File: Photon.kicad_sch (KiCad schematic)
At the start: 55 parts, among them J1 USB_C_Receptacle_USB2.0_14P, Q1 IRLML6402, Q2 IRLML6402, SW1 TS-1088-AR02016, U1 ATtiny13A-S, U2 RT8059GJ5, U3 TP4056, U4 BCR421UW6-7, U5 DW01A, U6 FS8205A, U7 BCR421UW6-7

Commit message: Updated
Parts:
- C1, C2: value 4.7uF -> 10uF
- C7: value 0.1uF -> 100nF
- R18: value 10K -> 100K
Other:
- note added: "Voltage Regulator 3V3"
- note removed: "Voltage Regulator 3V6"
- moved on the sheet: BT1, C3, C6, C7, D1, D2, Q2, R10, R14, R17, R19, R7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

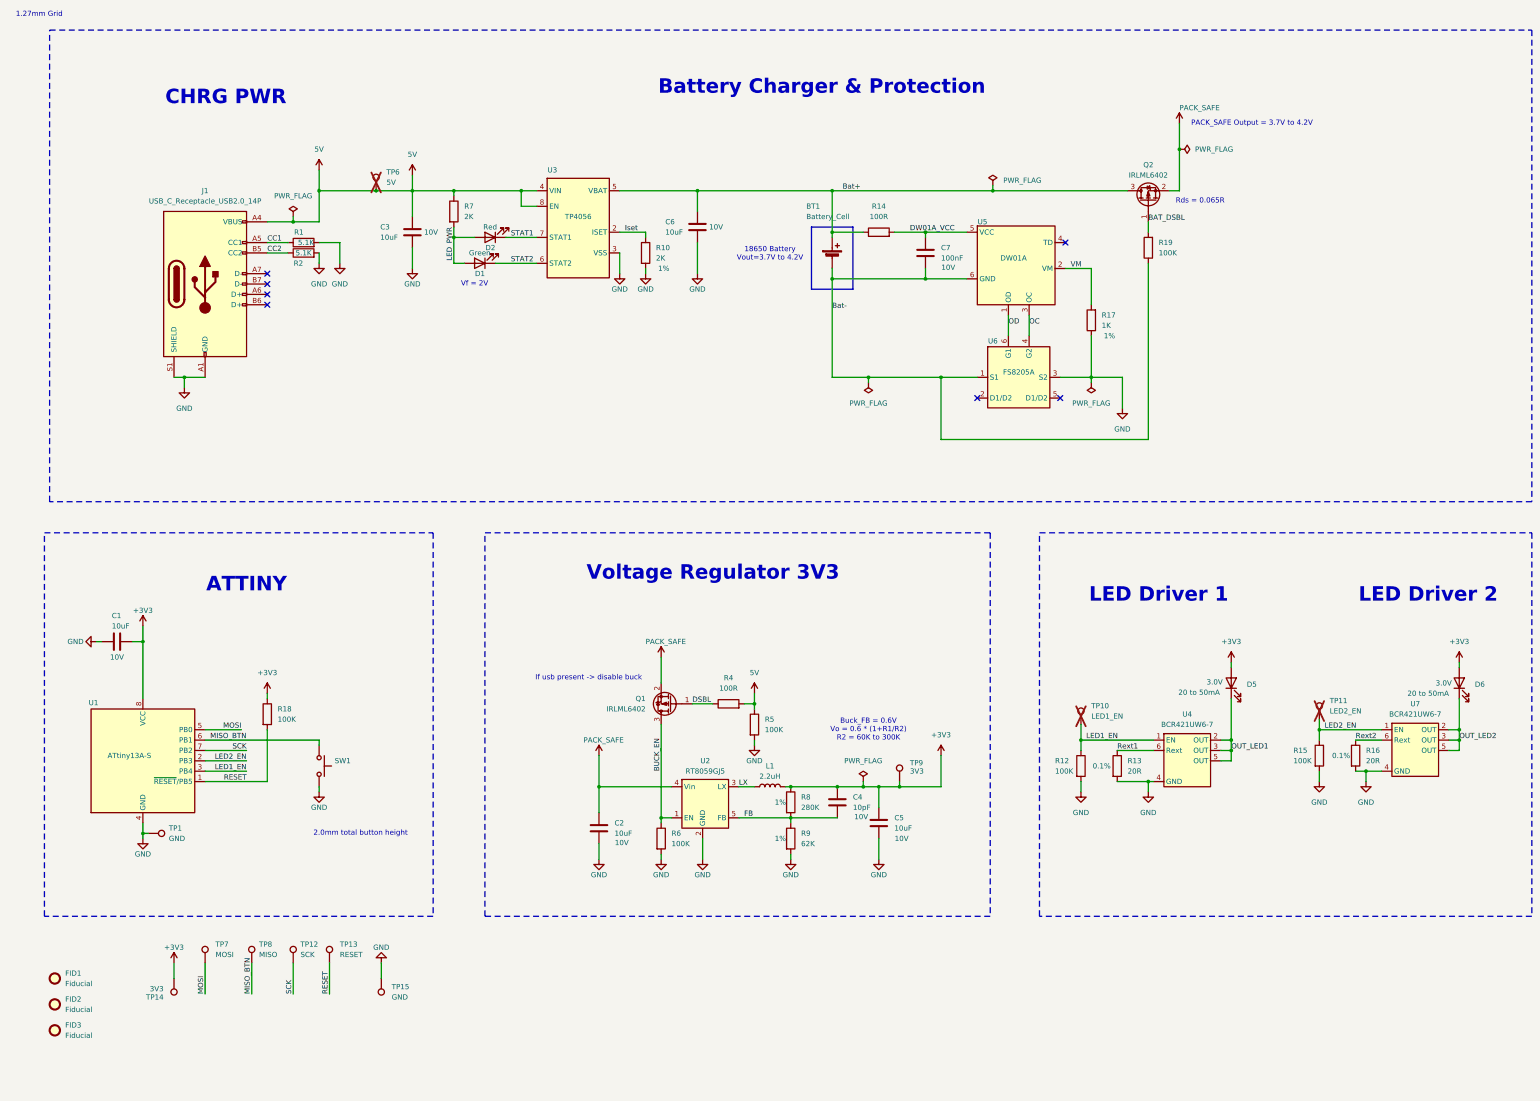
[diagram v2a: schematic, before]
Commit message: removing un needed parts
- pulldowns on LEDs
- pulldown on Buck
- cleaned up schematic
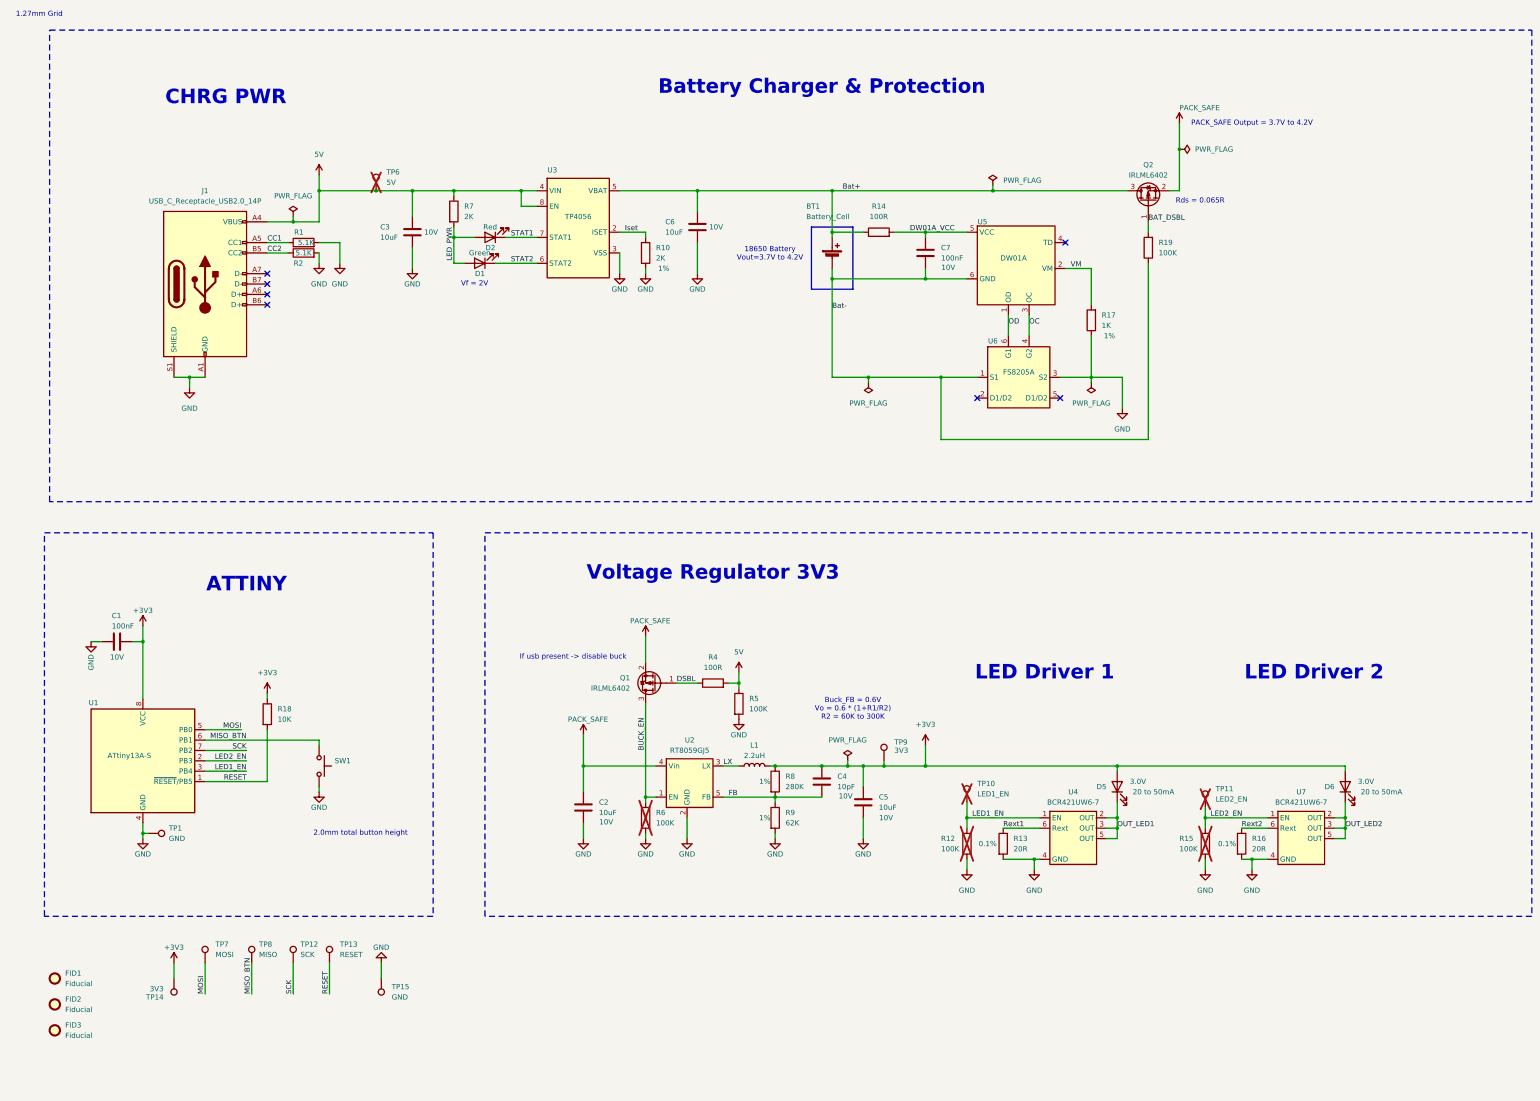
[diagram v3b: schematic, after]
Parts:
- C1: value 10uF -> 100nF
- R12, R15, R6: now not fitted
- R18: value 100K -> 10K
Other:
- moved on the sheet: C2, C4, C5, D5, D6, L1, Q1, R13, R16, R4, R5, R8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

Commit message: Swapped out MCU
- not completed (WIP)
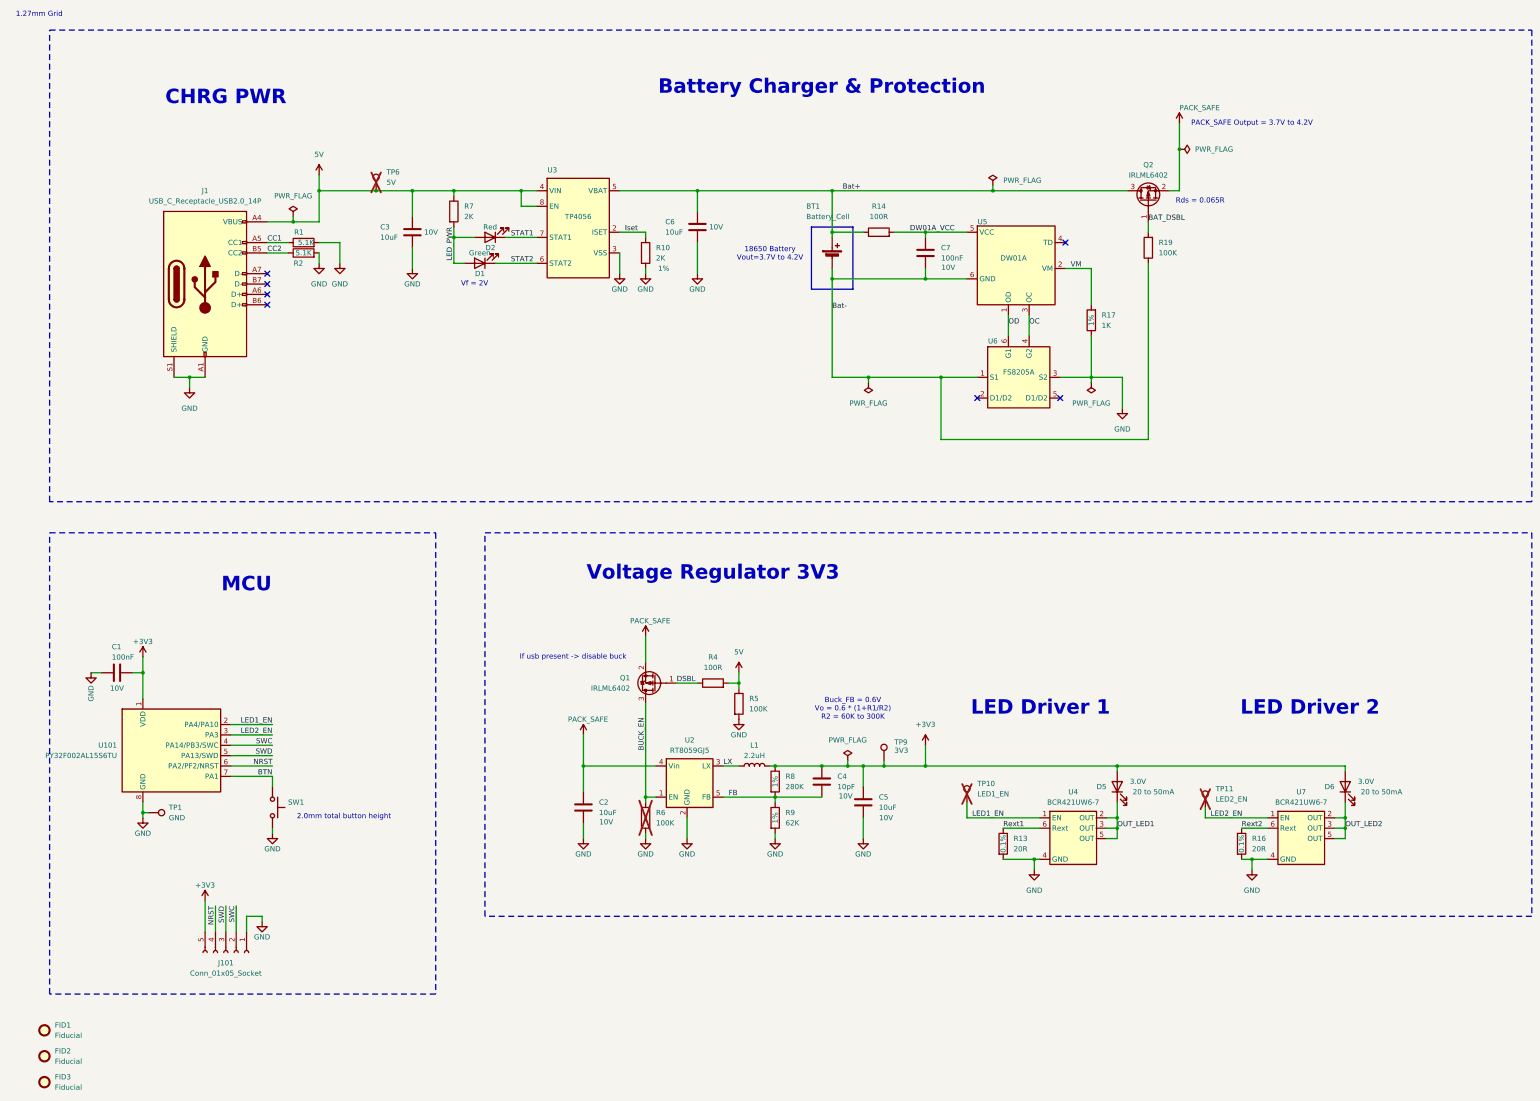
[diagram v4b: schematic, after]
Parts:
- removed R12, R15: 100K, Resistor_SMD:R_0603_1608Metric, symbol Device:R
- removed R18: 10K, Resistor_SMD:R_0603_1608Metric, symbol Device:R
- removed TP12: SCK, TestPoint:TestPoint_Pad_D1.0mm, symbol Connector:TestPoint
- removed TP13: RESET, TestPoint:TestPoint_Pad_D1.0mm, symbol Connector:TestPoint
- removed TP14: 3V3, TestPoint:TestPoint_THTPad_D1.0mm_Drill0.5mm, symbol Connector:TestPoint
- removed TP15: GND, TestPoint:TestPoint_Pad_D1.0mm, symbol Connector:TestPoint
- removed TP7: MOSI, TestPoint:TestPoint_Pad_D1.0mm, symbol Connector:TestPoint
- removed TP8: MISO, TestPoint:TestPoint_Pad_D1.0mm, symbol Connector:TestPoint
- removed U1: ATtiny13A-S, Package_SO:SO-8_3.9x4.9mm_P1.27mm, symbol MCU_Microchip_ATtiny:ATtiny13A-S
- added J101: Conn_01x05_Socket, symbol Connector:Conn_01x05_Socket
- added U101: PY32F002AL15S6TU, Package_SO:SOP-8_3.9x4.9mm_P1.27mm, symbol Photon:PY32F002AL15S6TU
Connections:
- net +3V3: now also J101.5 (Pin_5), U101.1 (VDD)
- net GND: now also J101.1 (Pin_1), U101.8 (GND)
- net LED1_EN: now also U101.2 (PA4/PA10)
- net LED2_EN: now also U101.3 (PA3)
- net MISO_BTN renamed BTN
- net BTN: now also U101.7 (PA1)
- new net NRST: J101.4 (Pin_4), U101.6 (PA2/PF2/NRST)
- new net SWC: J101.2 (Pin_2), U101.4 (PA14/PB3/SWC)
- new net SWD: J101.3 (Pin_3), U101.5 (PA13/SWD)
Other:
- note added: "MCU"
- note removed: "ATTINY"
- moved on the sheet: C1, FID1, FID2, FID3, SW1, TP1

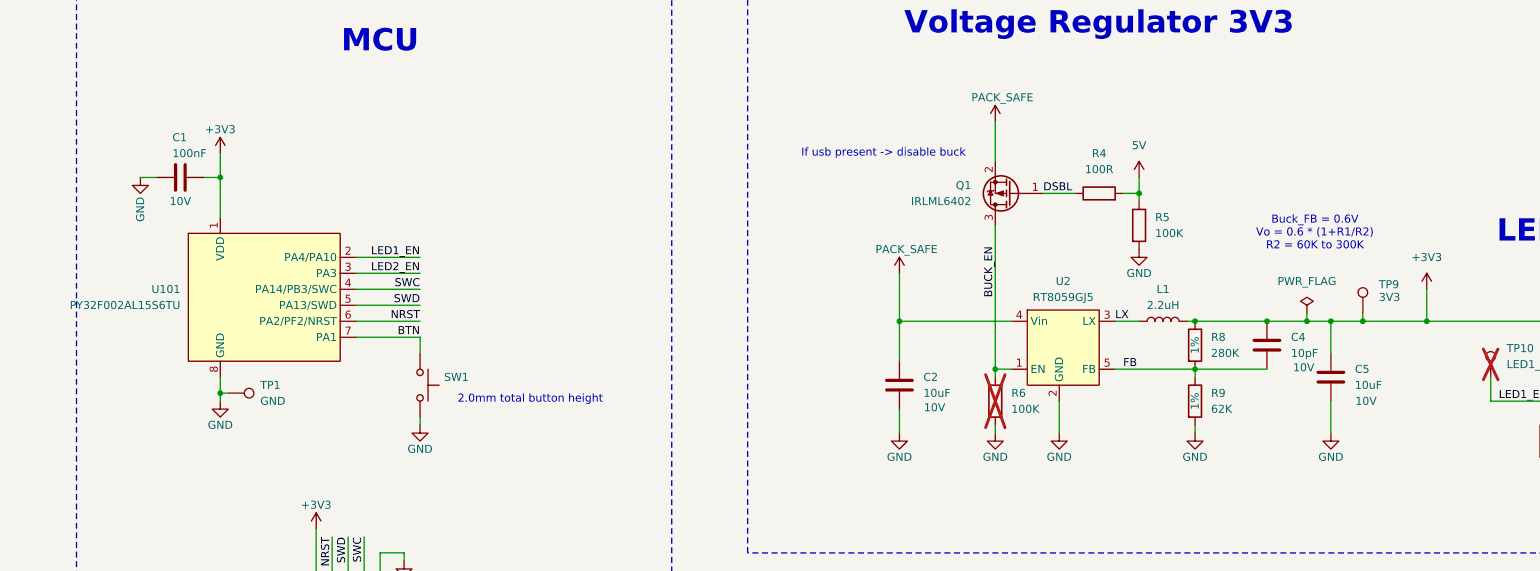
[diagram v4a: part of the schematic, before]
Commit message: Updated schem and PCB. updated footprints
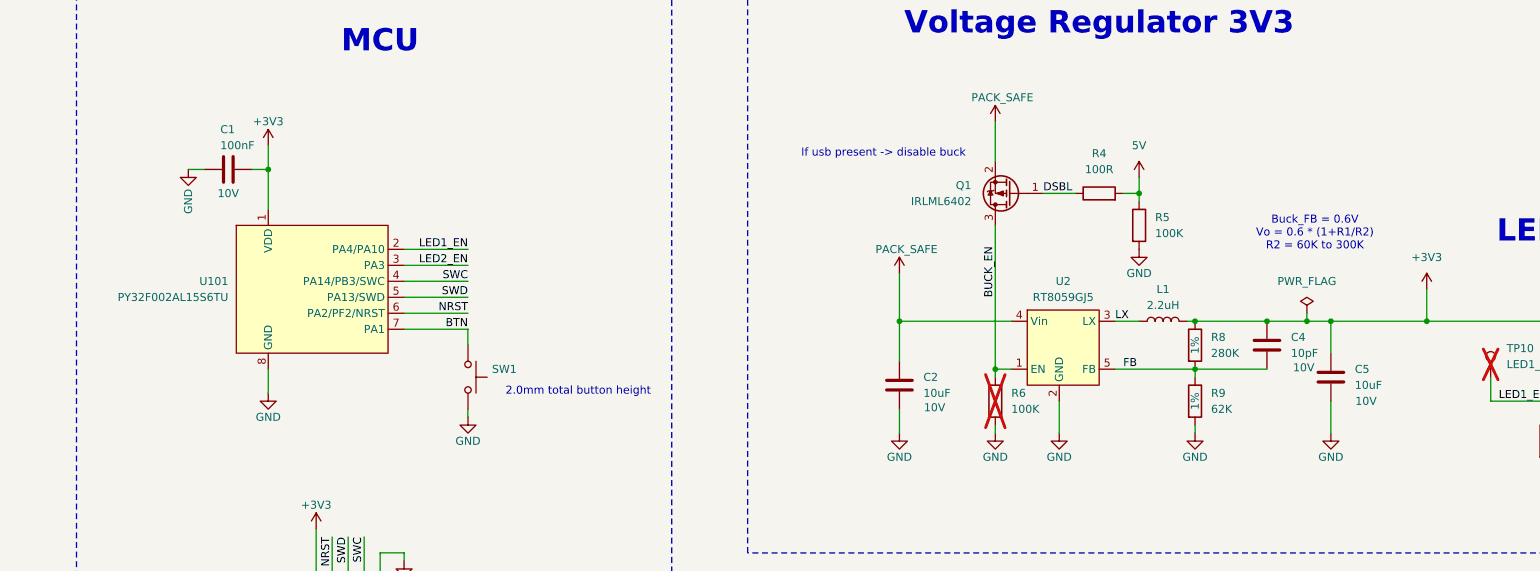
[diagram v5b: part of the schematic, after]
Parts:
- removed TP1: GND, TestPoint:TestPoint_Pad_D1.0mm, symbol Connector:TestPoint
- removed TP9: 3V3, TestPoint:TestPoint_Pad_D1.0mm, symbol Connector:TestPoint
- J101: footprint (none) -> Connector_PinHeader_2.54mm:PinHeader_1x05_P2.54mm_Vertical
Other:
- moved on the sheet: C1, SW1, U101

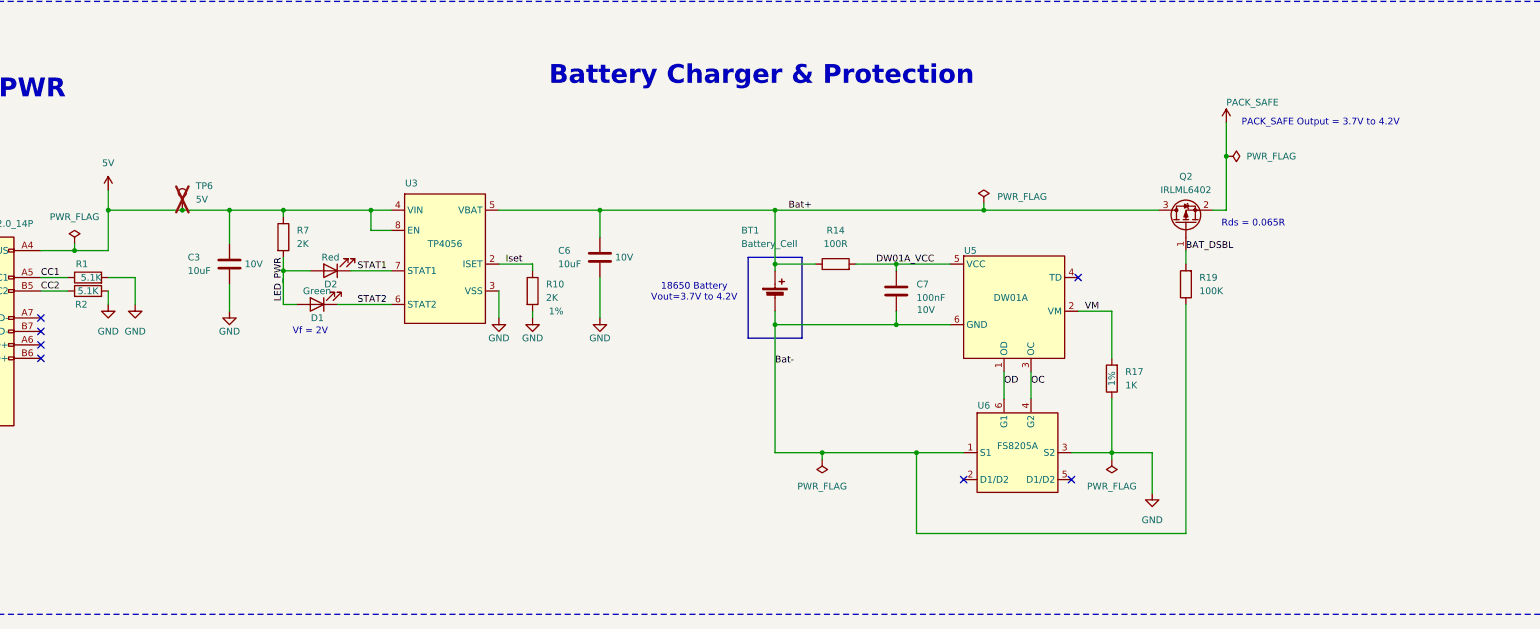
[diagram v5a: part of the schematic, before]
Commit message: added stitching vias and bi direction led for charging
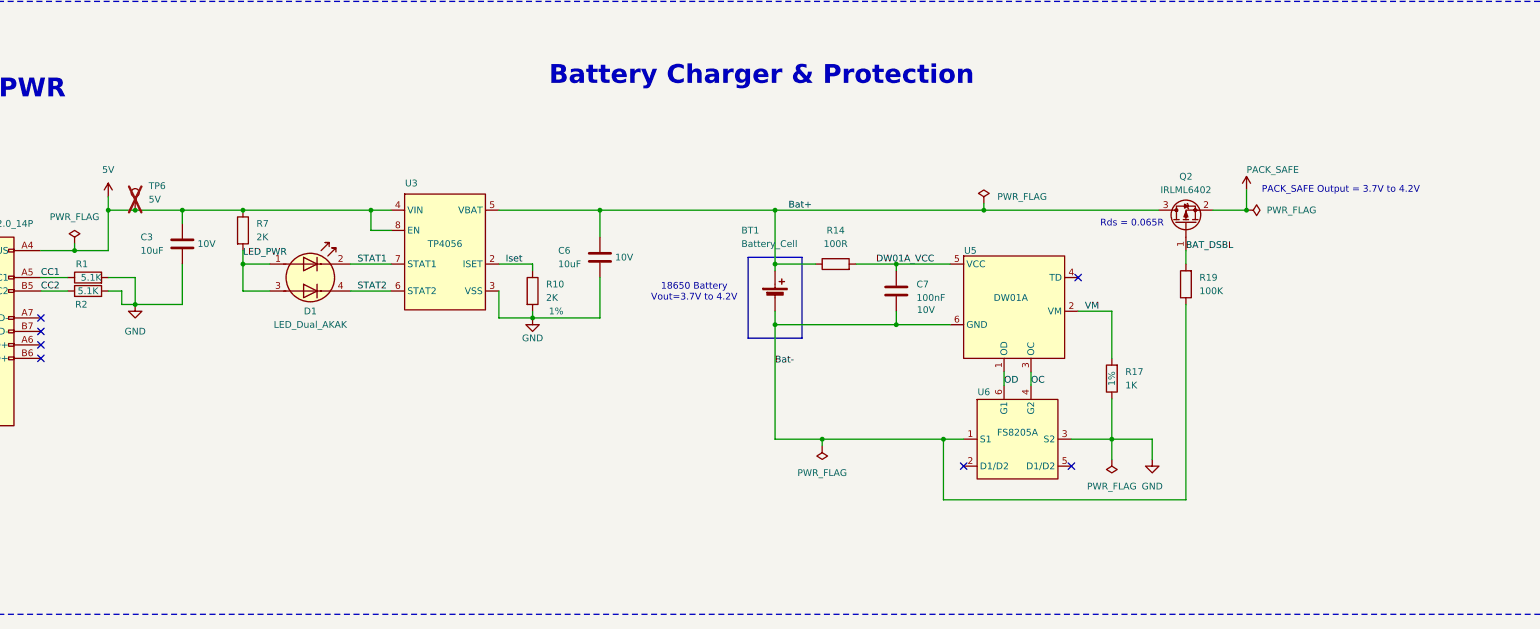
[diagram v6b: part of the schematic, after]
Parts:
- removed D1, D2: SZYY0603R1, LED_SMD:LED_0603_1608Metric, symbol Device:LED
- added D1: LED_Dual_AKAK, Photon:3.9mm Bi directional side mount LED, symbol Device:LED_Dual_AKAK
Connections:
- net LED_PWR: now also D1.1 (A1), D1.3 (A2)
- net STAT1: now also D1.2 (K1)
- net STAT2: now also D1.4 (K2)
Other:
- note removed: "Vf = 2V"
- moved on the sheet: C3, R7, TP6, U3, U6
